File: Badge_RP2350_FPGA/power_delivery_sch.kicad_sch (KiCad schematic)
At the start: 28 parts, among them J1 USB_C_Receptacle_USB2.0_16P, SW12 On/Off, U3 ME6211C12, U4 TMI7003C

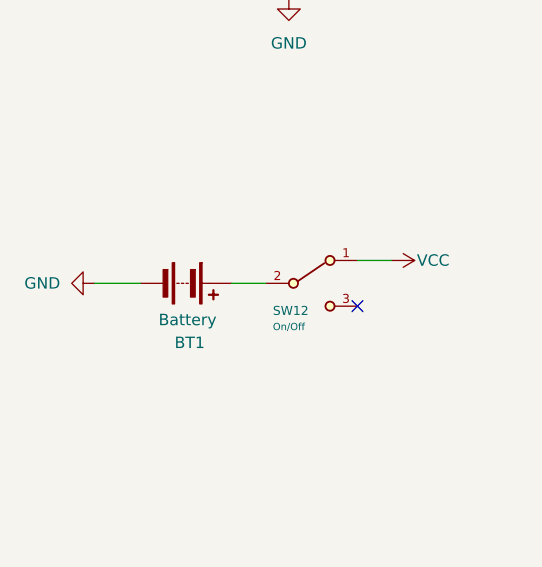
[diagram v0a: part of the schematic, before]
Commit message: M: pcb routing start, minor schematic changes
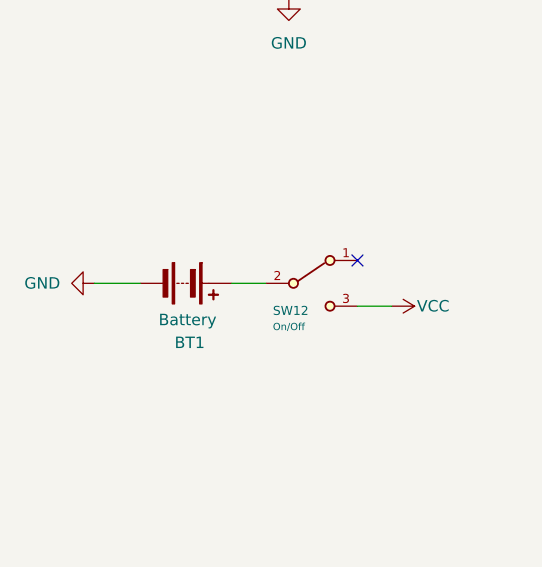
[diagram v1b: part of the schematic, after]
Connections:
- net VCC: now also SW12.3 (C); no longer SW12.1 (A)
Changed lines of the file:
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@@
 	)
 	(no_connect
-		(at 212.09 127)
+		(at 125.73 162.56)
 	)
 	(no_connect
-		(at 125.73 162.56)
+		(at 212.09 121.92)
 	)
 	(no_connect
@@
 	(wire
 		(pts
+			(xy 215.9 127) (xy 212.09 127)
+		)
+		(stroke
+			(width 0)
+			(type default)
+		)
+	)
+	(wire
+		(pts
 			(xy 140.97 58.42) (xy 140.97 60.96)
 		)
@@
 	(wire
 		(pts
-			(xy 215.9 121.92) (xy 212.09 121.92)
-		)
-		(stroke
-			(width 0)
-			(type default)
-		)
-	)
-	(wire
-		(pts
 			(xy 161.29 81.28) (xy 171.45 81.28)
 		)
@@
 	)
 	(symbol
-		(lib_id "power:VCC")
-		(at 215.9 121.92 270)
-		(unit 1)
-		(body_style 1)
-		(exclude_from_sim no)
-		(in_bom yes)
-		(on_board yes)
-		(in_pos_files yes)
-		(dnp no)
-		(property "Reference" "#PWR058"
-			(at 212.09 121.92 0)
-			(hide yes)
-			(show_name no)
-			(do_not_autoplace no)
-			(effects
-				(font
-					(size 1.27 1.27)
-				)
-			)
-		)
-		(property "Value" "VCC"
-			(at 218.694 121.92 90)
-			(show_name no)
-			(do_not_autoplace no)
-			(effects
-				(font
-					(size 1.27 1.27)
-				)
-				(justify left)
-			)
-		)
-		(property "Footprint" ""
-			(at 215.9 121.92 0)
-			(hide yes)
-			(show_name no)
-			(do_not_autoplace no)
-			(effects
-				(font
-					(size 1.27 1.27)
-				)
-			)
-		)
-		(property "Datasheet" ""
-			(at 215.9 121.92 0)
-			(hide yes)
-			(show_name no)
-			(do_not_autoplace no)
-			(effects
-				(font
-					(size 1.27 1.27)
-				)
-			)
-		)
-		(property "Description" "Power symbol creates a global label with name \"VCC\""
-			(at 215.9 121.92 0)
-			(hide yes)
-			(show_name no)
-			(do_not_autoplace no)
-			(effects
-				(font
-					(size 1.27 1.27)
-				)
-			)
-		)
-		(pin "1"
-		)
-		(instances
-			(project "Badge_RP2350_FPGA"
-				(path "/0ce87b49-0553-4a87-87c1-84e31180901e/d42deb57-951c-4ebe-afa1-91d9e0ce4651"
-					(reference "#PWR058")
-					(unit 1)
-				)
-			)
-		)
-	)
-	(symbol
 		(lib_id "Device:R")
 		(at 69.85 64.77 270)
@@
 					(unit 1)
 				)
+			)
+		)
+	)
+	(symbol
+		(lib_id "power:VCC")
+		(at 215.9 127 270)
+		(unit 1)
+		(body_style 1)
+		(exclude_from_sim no)
+		(in_bom yes)
+		(on_board yes)
+		(in_pos_files yes)
+		(dnp no)
+		(property "Reference" "#PWR058"
+			(at 212.09 127 0)
+			(hide yes)
+			(show_name no)
+			(do_not_autoplace no)
+			(effects
+				(font
+					(size 1.27 1.27)
+				)
+			)
+		)
+		(property "Value" "VCC"
+			(at 218.694 127 90)
+			(show_name no)
+			(do_not_autoplace no)
+			(effects
+				(font
+					(size 1.27 1.27)
+				)
+				(justify left)
+			)
+		)
+		(property "Footprint" ""
+			(at 215.9 127 0)
+			(hide yes)
+			(show_name no)
+			(do_not_autoplace no)
+			(effects
+				(font
+					(size 1.27 1.27)
+				)
+			)
+		)
+		(property "Datasheet" ""
+			(at 215.9 127 0)
+			(hide yes)
+			(show_name no)
+			(do_not_autoplace no)
+			(effects
+				(font
+					(size 1.27 1.27)
+				)
+			)
+		)
+		(property "Description" "Power symbol creates a global label with name \"VCC\""
+			(at 215.9 127 0)
+			(hide yes)
+			(show_name no)
+			(do_not_autoplace no)
+			(effects
+				(font
+					(size 1.27 1.27)
+				)
+			)
+		)
+		(pin "1"
+		)
+		(instances
+			(project "Badge_RP2350_FPGA"
+				(path "/0ce87b49-0553-4a87-87c1-84e31180901e/d42deb57-951c-4ebe-afa1-91d9e0ce4651"
+					(reference "#PWR058")
+					(unit 1)
+				)

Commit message: F: DRC and USB-C
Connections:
- net 5 v is gone; now on net VCC: U4.18 (EN3), U4.8 (EN2), U4.9 (EN1)
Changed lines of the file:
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@@
 	)
 	(junction
+		(at 140.97 46.99)
+		(diameter 0)
+		(color 0 0 0 0)
+	)
+	(junction
 		(at 113.03 76.2)
 		(diameter 0)
@@
 	)
 	(junction
+		(at 140.97 49.53)
+		(diameter 0)
+		(color 0 0 0 0)
+	)
+	(junction
 		(at 55.88 38.1)
 		(diameter 0)
@@
 	(wire
 		(pts
+			(xy 140.97 46.99) (xy 140.97 49.53)
+		)
+		(stroke
+			(width 0)
+			(type default)
+		)
+	)
+	(wire
+		(pts
 			(xy 125.73 134.62) (xy 133.35 134.62)
 		)
@@
 	(wire
 		(pts
-			(xy 134.62 46.99) (xy 144.78 46.99)
+			(xy 134.62 46.99) (xy 140.97 46.99)
 		)
 		(stroke
@@
 	(wire
 		(pts
+			(xy 140.97 46.99) (xy 144.78 46.99)
+		)
+		(stroke
+			(width 0)
+			(type default)
+		)
+	)
+	(wire
+		(pts
 			(xy 85.09 44.45) (xy 81.28 44.45)
 		)
@@
 					(unit 1)
 				)
-			)
-		)
-	)
-	(symbol
-		(lib_id "power:VCC")
-		(at 140.97 52.07 270)
-		(unit 1)
-		(body_style 1)
-		(exclude_from_sim no)
-		(in_bom yes)
-		(on_board yes)
-		(in_pos_files yes)
-		(dnp no)
-		(property "Reference" "#PWR08"
-			(at 137.16 52.07 0)
-			(hide yes)
-			(show_name no)
-			(do_not_autoplace no)
-			(effects
-				(font
-					(size 1.27 1.27)
-				)
-			)
-		)
-		(property "Value" "5 v"
-			(at 143.51 53.594 90)
-			(show_name no)
-			(do_not_autoplace no)
-			(effects
-				(font
-					(size 1.27 1.27)
-				)
-				(justify left)
-			)
-		)
-		(property "Footprint" ""
-			(at 140.97 52.07 0)
-			(hide yes)
-			(show_name no)
-			(do_not_autoplace no)
-			(effects
-				(font
-					(size 1.27 1.27)
-				)
-			)
-		)
-		(property "Datasheet" ""
-			(at 140.97 52.07 0)
-			(hide yes)
-			(show_name no)
-			(do_not_autoplace no)
-			(effects
-				(font
-					(size 1.27 1.27)
-				)
-			)
-		)
-		(property "Description" "Power symbol creates a global label with name \"VCC\""
-			(at 140.97 52.07 0)
-			(hide yes)
-			(show_name no)
-			(do_not_autoplace no)
-			(effects
-				(font
-					(size 1.27 1.27)
-				)
-			)
-		)
-		(pin "1"
-		)
-		(instances
-			(project "Badge_RP2350_FPGA"
-				(path "/0ce87b49-0553-4a87-87c1-84e31180901e/d42deb57-951c-4ebe-afa1-91d9e0ce4651"
-					(reference "#PWR08")
-					(unit 1)
-				)

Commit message: fixes
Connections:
- net VCC renamed VBUS
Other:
- moved on the sheet: C47, C48
